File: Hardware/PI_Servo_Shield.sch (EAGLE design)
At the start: 80 parts, among them J1 RASPBERRYPI-40-PIN-GPIO, J19 QWIIC, J20 USB C, J21 Serial, Q1 2N7002PW, Q4 2N7002PW, U1 PCA9685, U3 CH340C

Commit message: Bumped the QWIIC label to 5mm package
didn't print very cleanly at the 3mm size on the protos from jlcpcb, so bumped it up to 5mm package.
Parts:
- U$1: value QWIIC_LOGO_3MM -> QWIIC_LOGO_5MM; device SparkFun-Aesthetics:QWIIC_LOGO_3MM -> SparkFun-Aesthetics:QWIIC_LOGO_5MM
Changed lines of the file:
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@@
 <grid distance="0.1" unitdist="inch" unit="inch" style="lines" multiple="1" display="no" altdistance="0.01" altunitdist="inch" altunit="inch"/>
 <layers>
-<layer number="1" name="Top" color="4" fill="1" visible="no" active="no"/>
-<layer number="2" name="Route2" color="1" fill="3" visible="no" active="no"/>
-<layer number="3" name="Route3" color="4" fill="3" visible="no" active="no"/>
-<layer number="4" name="Route4" color="1" fill="4" visible="no" active="no"/>
-<layer number="5" name="Route5" color="4" fill="4" visible="no" active="no"/>
-<layer number="6" name="Route6" color="1" fill="8" visible="no" active="no"/>
-<layer number="7" name="Route7" color="4" fill="8" visible="no" active="no"/>
-<layer number="8" name="Route8" color="1" fill="2" visible="no" active="no"/>
-<layer number="9" name="Route9" color="4" fill="2" visible="no" active="no"/>
-<layer number="10" name="Route10" color="1" fill="7" visible="no" active="no"/>
-<layer number="11" name="Route11" color="4" fill="7" visible="no" active="no"/>
-<layer number="12" name="Route12" color="1" fill="5" visible="no" active="no"/>
-<layer number="13" name="Route13" color="4" fill="5" visible="no" active="no"/>
-<layer number="14" name="Route14" color="1" fill="6" visible="no" active="no"/>
-<layer number="15" name="Route15" color="4" fill="6" visible="no" active="no"/>
-<layer number="16" name="Bottom" color="1" fill="1" visible="no" active="no"/>
-<layer number="17" name="Pads" color="2" fill="1" visible="no" active="no"/>
-<layer number="18" name="Vias" color="2" fill="1" visible="no" active="no"/>
-<layer number="19" name="Unrouted" color="6" fill="1" visible="no" active="no"/>
-<layer number="20" name="Dimension" color="15" fill="1" visible="no" active="no"/>
-<layer number="21" name="tPlace" color="16" fill="1" visible="no" active="no"/>
-<layer number="22" name="bPlace" color="14" fill="1" visible="no" active="no"/>
-<layer number="23" name="tOrigins" color="15" fill="1" visible="no" active="no"/>
-<layer number="24" name="bOrigins" color="15" fill="1" visible="no" active="no"/>
-<layer number="25" name="tNames" color="7" fill="1" visible="no" active="no"/>
-<layer number="26" name="bNames" color="7" fill="1" visible="no" active="no"/>
-<layer number="27" name="tValues" color="7" fill="1" visible="no" active="no"/>
-<layer number="28" name="bValues" color="7" fill="1" visible="no" active="no"/>
+<layer number="1" name="Top" color="4" fill="1" visible="yes" active="no"/>
+<layer number="2" name="Route2" color="1" fill="3" visible="yes" active="no"/>
+<layer number="3" name="Route3" color="4" fill="3" visible="yes" active="no"/>
+<layer number="4" name="Route4" color="1" fill="4" visible="yes" active="no"/>
+<layer number="5" name="Route5" color="4" fill="4" visible="yes" active="no"/>
+<layer number="6" name="Route6" color="1" fill="8" visible="yes" active="no"/>
+<layer number="7" name="Route7" color="4" fill="8" visible="yes" active="no"/>
+<layer number="8" name="Route8" color="1" fill="2" visible="yes" active="no"/>
+<layer number="9" name="Route9" color="4" fill="2" visible="yes" active="no"/>
+<layer number="10" name="Route10" color="1" fill="7" visible="yes" active="no"/>
+<layer number="11" name="Route11" color="4" fill="7" visible="yes" active="no"/>
+<layer number="12" name="Route12" color="1" fill="5" visible="yes" active="no"/>
+<layer number="13" name="Route13" color="4" fill="5" visible="yes" active="no"/>
+<layer number="14" name="Route14" color="1" fill="6" visible="yes" active="no"/>
+<layer number="15" name="Route15" color="4" fill="6" visible="yes" active="no"/>
+<layer number="16" name="Bottom" color="1" fill="1" visible="yes" active="no"/>
+<layer number="17" name="Pads" color="2" fill="1" visible="yes" active="no"/>
+<layer number="18" name="Vias" color="2" fill="1" visible="yes" active="no"/>
+<layer number="19" name="Unrouted" color="6" fill="1" visible="yes" active="no"/>
+<layer number="20" name="Dimension" color="15" fill="1" visible="yes" active="no"/>
+<layer number="21" name="tPlace" color="16" fill="1" visible="yes" active="no"/>
+<layer number="22" name="bPlace" color="14" fill="1" visible="yes" active="no"/>
+<layer number="23" name="tOrigins" color="15" fill="1" visible="yes" active="no"/>
+<layer number="24" name="bOrigins" color="15" fill="1" visible="yes" active="no"/>
+<layer number="25" name="tNames" color="7" fill="1" visible="yes" active="no"/>
+<layer number="26" name="bNames" color="7" fill="1" visible="yes" active="no"/>
+<layer number="27" name="tValues" color="7" fill="1" visible="yes" active="no"/>
+<layer number="28" name="bValues" color="7" fill="1" visible="yes" active="no"/>
 <layer number="29" name="tStop" color="7" fill="3" visible="no" active="no"/>
 <layer number="30" name="bStop" color="7" fill="6" visible="no" active="no"/>
@@
 <layer number="35" name="tGlue" color="7" fill="4" visible="no" active="no"/>
 <layer number="36" name="bGlue" color="7" fill="5" visible="no" active="no"/>
-<layer number="37" name="tTest" color="7" fill="1" visible="no" active="no"/>
-<layer number="38" name="bTest" color="7" fill="1" visible="no" active="no"/>
+<layer number="37" name="tTest" color="7" fill="1" visible="yes" active="no"/>
+<layer number="38" name="bTest" color="7" fill="1" visible="yes" active="no"/>
 <layer number="39" name="tKeepout" color="4" fill="11" visible="no" active="no"/>
 <layer number="40" name="bKeepout" color="1" fill="11" visible="no" active="no"/>
@@
 <layer number="44" name="Drills" color="7" fill="1" visible="no" active="no"/>
 <layer number="45" name="Holes" color="7" fill="1" visible="no" active="no"/>
-<layer number="46" name="Milling" color="3" fill="1" visible="no" active="no"/>
-<layer number="47" name="Measures" color="7" fill="1" visible="no" active="no"/>
-<layer number="48" name="Document" color="7" fill="1" visible="no" active="no"/>
-<layer number="49" name="Reference" color="7" fill="1" visible="no" active="no"/>
-<layer number="50" name="dxf" color="7" fill="1" visible="no" active="no"/>
-<layer number="51" name="tDocu" color="6" fill="1" visible="no" active="no"/>
-<layer number="52" name="bDocu" color="7" fill="1" visible="no" active="no"/>
-<layer number="53" name="tGND_GNDA" color="7" fill="9" visible="no" active="no"/>
-<layer number="54" name="bGND_GNDA" color="1" fill="9" visible="no" active="no"/>
-<layer number="56" name="wert" color="7" fill="1" visible="no" active="no"/>
-<layer number="57" name="tCAD" color="7" fill="1" visible="no" active="no"/>
-<layer number="59" name="tCarbon" color="7" fill="1" visible="no" active="no"/>
-<layer number="60" name="bCarbon" color="7" fill="1" visible="no" active="no"/>
+<layer number="46" name="Milling" color="3" fill="1" visible="yes" active="no"/>
+<layer number="47" name="Measures" color="7" fill="1" visible="yes" active="no"/>
+<layer number="48" name="Document" color="62" fill="7" visible="yes" active="no"/>
+<layer number="49" name="Reference" color="7" fill="1" visible="yes" active="no"/>
+<layer number="50" name="dxf" color="7" fill="1" visible="yes" active="no"/>
+<layer number="51" name="tDocu" color="6" fill="1" visible="yes" active="no"/>
+<layer number="52" name="bDocu" color="7" fill="1" visible="yes" active="no"/>
+<layer number="53" name="tGND_GNDA" color="7" fill="9" visible="yes" active="no"/>
+<layer number="54" name="bGND_GNDA" color="1" fill="9" visible="yes" active="no"/>
+<layer number="56" name="wert" color="7" fill="1" visible="yes" active="no"/>
+<layer number="57" name="tCAD" color="7" fill="1" visible="yes" active="no"/>
+<layer number="59" name="tCarbon" color="7" fill="1" visible="yes" active="no"/>
+<layer number="60" name="bCarbon" color="7" fill="1" visible="yes" active="no"/>
 <layer number="88" name="SimResults" color="9" fill="1" visible="no" active="yes"/>
 <layer number="89" name="SimProbes" color="9" fill="1" visible="no" active="yes"/>
@@
 <part name="GND1" library="SparkFun-PowerSymbols" deviceset="GND" device=""/>
 <part name="J21" library="SparkFun-Connectors" deviceset="CONN_04" device="LOCK" value="Serial"/>
-<part name="U$1" library="SparkFun-Aesthetics" deviceset="QWIIC_LOGO" device="_3MM"/>
+<part name="U$1" library="SparkFun-Aesthetics" deviceset="QWIIC_LOGO" device="_5MM" value="QWIIC_LOGO_5MM"/>
 <part name="C10" library="SparkFun-Capacitors" deviceset="0.1UF" device="-0603-25V-(+80/-20%)" value="0.1uF"/>
 <part name="GND24" library="SparkFun-PowerSymbols" deviceset="GND" device=""/>

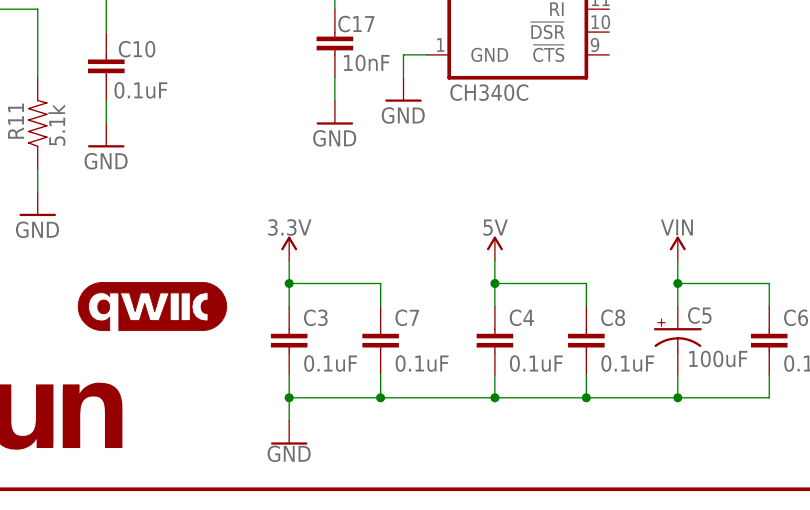
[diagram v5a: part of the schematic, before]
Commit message: Added 3.3V test point - gonna need this for properly testing the CH340
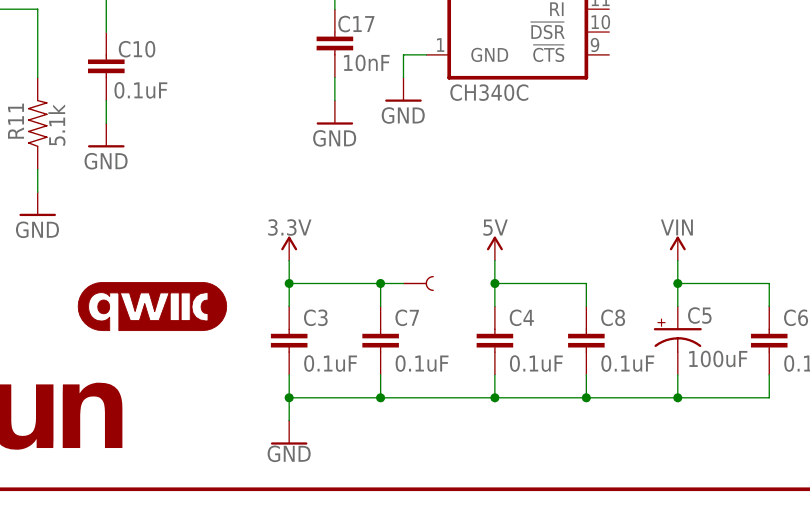
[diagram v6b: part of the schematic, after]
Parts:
- added TP22: TEST-POINT3X4, SparkFun-Connectors:TEST-POINT3X4
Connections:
- net 3.3V: now also TP22.1
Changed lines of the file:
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@@
 <grid distance="0.1" unitdist="inch" unit="inch" style="lines" multiple="1" display="no" altdistance="0.01" altunitdist="inch" altunit="inch"/>
 <layers>
-<layer number="1" name="Top" color="4" fill="1" visible="yes" active="no"/>
-<layer number="2" name="Route2" color="1" fill="3" visible="yes" active="no"/>
-<layer number="3" name="Route3" color="4" fill="3" visible="yes" active="no"/>
-<layer number="4" name="Route4" color="1" fill="4" visible="yes" active="no"/>
-<layer number="5" name="Route5" color="4" fill="4" visible="yes" active="no"/>
-<layer number="6" name="Route6" color="1" fill="8" visible="yes" active="no"/>
-<layer number="7" name="Route7" color="4" fill="8" visible="yes" active="no"/>
-<layer number="8" name="Route8" color="1" fill="2" visible="yes" active="no"/>
-<layer number="9" name="Route9" color="4" fill="2" visible="yes" active="no"/>
-<layer number="10" name="Route10" color="1" fill="7" visible="yes" active="no"/>
-<layer number="11" name="Route11" color="4" fill="7" visible="yes" active="no"/>
-<layer number="12" name="Route12" color="1" fill="5" visible="yes" active="no"/>
-<layer number="13" name="Route13" color="4" fill="5" visible="yes" active="no"/>
-<layer number="14" name="Route14" color="1" fill="6" visible="yes" active="no"/>
-<layer number="15" name="Route15" color="4" fill="6" visible="yes" active="no"/>
-<layer number="16" name="Bottom" color="1" fill="1" visible="yes" active="no"/>
-<layer number="17" name="Pads" color="2" fill="1" visible="yes" active="no"/>
-<layer number="18" name="Vias" color="2" fill="1" visible="yes" active="no"/>
-<layer number="19" name="Unrouted" color="6" fill="1" visible="yes" active="no"/>
-<layer number="20" name="Dimension" color="15" fill="1" visible="yes" active="no"/>
-<layer number="21" name="tPlace" color="16" fill="1" visible="yes" active="no"/>
-<layer number="22" name="bPlace" color="14" fill="1" visible="yes" active="no"/>
-<layer number="23" name="tOrigins" color="15" fill="1" visible="yes" active="no"/>
-<layer number="24" name="bOrigins" color="15" fill="1" visible="yes" active="no"/>
-<layer number="25" name="tNames" color="7" fill="1" visible="yes" active="no"/>
-<layer number="26" name="bNames" color="7" fill="1" visible="yes" active="no"/>
-<layer number="27" name="tValues" color="7" fill="1" visible="yes" active="no"/>
-<layer number="28" name="bValues" color="7" fill="1" visible="yes" active="no"/>
+<layer number="1" name="Top" color="4" fill="1" visible="no" active="no"/>
+<layer number="2" name="Route2" color="1" fill="3" visible="no" active="no"/>
+<layer number="3" name="Route3" color="4" fill="3" visible="no" active="no"/>
+<layer number="4" name="Route4" color="1" fill="4" visible="no" active="no"/>
+<layer number="5" name="Route5" color="4" fill="4" visible="no" active="no"/>
+<layer number="6" name="Route6" color="1" fill="8" visible="no" active="no"/>
+<layer number="7" name="Route7" color="4" fill="8" visible="no" active="no"/>
+<layer number="8" name="Route8" color="1" fill="2" visible="no" active="no"/>
+<layer number="9" name="Route9" color="4" fill="2" visible="no" active="no"/>
+<layer number="10" name="Route10" color="1" fill="7" visible="no" active="no"/>
+<layer number="11" name="Route11" color="4" fill="7" visible="no" active="no"/>
+<layer number="12" name="Route12" color="1" fill="5" visible="no" active="no"/>
+<layer number="13" name="Route13" color="4" fill="5" visible="no" active="no"/>
+<layer number="14" name="Route14" color="1" fill="6" visible="no" active="no"/>
+<layer number="15" name="Route15" color="4" fill="6" visible="no" active="no"/>
+<layer number="16" name="Bottom" color="1" fill="1" visible="no" active="no"/>
+<layer number="17" name="Pads" color="2" fill="1" visible="no" active="no"/>
+<layer number="18" name="Vias" color="2" fill="1" visible="no" active="no"/>
+<layer number="19" name="Unrouted" color="6" fill="1" visible="no" active="no"/>
+<layer number="20" name="Dimension" color="15" fill="1" visible="no" active="no"/>
+<layer number="21" name="tPlace" color="16" fill="1" visible="no" active="no"/>
+<layer number="22" name="bPlace" color="14" fill="1" visible="no" active="no"/>
+<layer number="23" name="tOrigins" color="15" fill="1" visible="no" active="no"/>
+<layer number="24" name="bOrigins" color="15" fill="1" visible="no" active="no"/>
+<layer number="25" name="tNames" color="7" fill="1" visible="no" active="no"/>
+<layer number="26" name="bNames" color="7" fill="1" visible="no" active="no"/>
+<layer number="27" name="tValues" color="7" fill="1" visible="no" active="no"/>
+<layer number="28" name="bValues" color="7" fill="1" visible="no" active="no"/>
 <layer number="29" name="tStop" color="7" fill="3" visible="no" active="no"/>
 <layer number="30" name="bStop" color="7" fill="6" visible="no" active="no"/>
@@
 <layer number="35" name="tGlue" color="7" fill="4" visible="no" active="no"/>
 <layer number="36" name="bGlue" color="7" fill="5" visible="no" active="no"/>
-<layer number="37" name="tTest" color="7" fill="1" visible="yes" active="no"/>
-<layer number="38" name="bTest" color="7" fill="1" visible="yes" active="no"/>
+<layer number="37" name="tTest" color="7" fill="1" visible="no" active="no"/>
+<layer number="38" name="bTest" color="7" fill="1" visible="no" active="no"/>
 <layer number="39" name="tKeepout" color="4" fill="11" visible="no" active="no"/>
 <layer number="40" name="bKeepout" color="1" fill="11" visible="no" active="no"/>
@@
 <layer number="44" name="Drills" color="7" fill="1" visible="no" active="no"/>
 <layer number="45" name="Holes" color="7" fill="1" visible="no" active="no"/>
-<layer number="46" name="Milling" color="3" fill="1" visible="yes" active="no"/>
-<layer number="47" name="Measures" color="7" fill="1" visible="yes" active="no"/>
-<layer number="48" name="Document" color="62" fill="7" visible="yes" active="no"/>
-<layer number="49" name="Reference" color="7" fill="1" visible="yes" active="no"/>
-<layer number="50" name="dxf" color="7" fill="1" visible="yes" active="no"/>
-<layer number="51" name="tDocu" color="6" fill="1" visible="yes" active="no"/>
-<layer number="52" name="bDocu" color="7" fill="1" visible="yes" active="no"/>
-<layer number="53" name="tGND_GNDA" color="7" fill="9" visible="yes" active="no"/>
-<layer number="54" name="bGND_GNDA" color="1" fill="9" visible="yes" active="no"/>
-<layer number="56" name="wert" color="7" fill="1" visible="yes" active="no"/>
-<layer number="57" name="tCAD" color="7" fill="1" visible="yes" active="no"/>
-<layer number="59" name="tCarbon" color="7" fill="1" visible="yes" active="no"/>
-<layer number="60" name="bCarbon" color="7" fill="1" visible="yes" active="no"/>
+<layer number="46" name="Milling" color="3" fill="1" visible="no" active="no"/>
+<layer number="47" name="Measures" color="7" fill="1" visible="no" active="no"/>
+<layer number="48" name="Document" color="62" fill="7" visible="no" active="no"/>
+<layer number="49" name="Reference" color="7" fill="1" visible="no" active="no"/>
+<layer number="50" name="dxf" color="7" fill="1" visible="no" active="no"/>
+<layer number="51" name="tDocu" color="6" fill="1" visible="no" active="no"/>
+<layer number="52" name="bDocu" color="7" fill="1" visible="no" active="no"/>
+<layer number="53" name="tGND_GNDA" color="7" fill="9" visible="no" active="no"/>
+<layer number="54" name="bGND_GNDA" color="1" fill="9" visible="no" active="no"/>
+<layer number="56" name="wert" color="7" fill="1" visible="no" active="no"/>
+<layer number="57" name="tCAD" color="7" fill="1" visible="no" active="no"/>
+<layer number="59" name="tCarbon" color="7" fill="1" visible="no" active="no"/>
+<layer number="60" name="bCarbon" color="7" fill="1" visible="no" active="no"/>
 <layer number="88" name="SimResults" color="9" fill="1" visible="no" active="yes"/>
 <layer number="89" name="SimProbes" color="9" fill="1" visible="no" active="yes"/>
@@
 <part name="Q4" library="SparkFun-DiscreteSemi" deviceset="MOSFET-NCH" device="-2N7002PW" value="2N7002PW"/>
 <part name="3.3V7" library="SparkFun-PowerSymbols" deviceset="VIN" device="" value="3.3V"/>
+<part name="TP22" library="SparkFun-Connectors" deviceset="TEST-POINT" device="3X4" value=""/>
 </parts>
 <sheets>
@@
 <attribute name="VALUE" x="198.12" y="145.034" size="1.778" layer="96" font="vector" rot="MR0" align="bottom-center"/>
 </instance>
+<instance part="TP22" gate="G$1" x="86.36" y="22.86" smashed="yes">
+<attribute name="VALUE" x="83.82" y="20.32" size="1.778" layer="96" font="vector"/>
+</instance>
 </instances>
 <busses>
@@
 <wire x1="73.66" y1="22.86" x2="73.66" y2="25.4" width="0.1524" layer="91"/>
 <junction x="73.66" y="22.86"/>
-</segment>
-<segment>
+<pinref part="TP22" gate="G$1" pin="1"/>
+<wire x1="86.36" y1="22.86" x2="83.82" y2="22.86" width="0.1524" layer="91"/>
+<junction x="83.82" y="22.86"/>
+</segment>
+<segment>

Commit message: Reverse current blocking diodes and more
-Added reverse current blocking circuits.
-Added auto switching isolation fet between Pi 5V rail and servo rail.
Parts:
- removed FRAME1: FRAME-LETTER, SparkFun-Aesthetics:FRAME-LETTER
- added FRAME2: FRAME-LEDGER, SparkFun-Aesthetics:FRAME-LEDGER
- added Q10, Q3, Q6, Q8: (no value), SparkFun-DiscreteSemi:TRANS_PNP_DUALSOT-363
- added Q11: (no value), SparkFun-DiscreteSemi:TRANS_NPN_DUAL-MBT3904DW1T1
- added Q12, Q2, Q5, Q7, Q9: 2.5A/30V/105mΩ, SparkFun-DiscreteSemi:MOSFET_PCH-DMG2307L
- added R13, R15, R19, R20, R21, R6, R8: 10k, SparkFun-Resistors:10KOHM-0603-1/10W-1%
- added R14, R3, R7, R9: 47k, SparkFun-Resistors:47KOHM-0603-1/10W-1%
- added R17, R18: 100, SparkFun-Resistors:100OHM-0603-1/4W-5%
- added S1: (no value), SparkFun-Switches:SWITCH-SPDT-PTH-11.6X4.0MM-LOCK
- added U2: SN74LVC1G32DCKR, SparkFun-IC-Logic:74LVC32DBV
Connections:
- net RXI renamed PI-TXO
- removed net 5V: C4.1, C8.1, J1.5V@2, J1.5V@4, J21.4, JP4.2, R1.2, R2.2, U1.VDD
- removed net TXO: D1.C, J1.RXI, J21.1, TP21.1, U3.TXO
- removed net VIN: C5.+, C6.1, F2.2, J10.2, J11.2, J12.2, J13.2, J14.2, J15.2, J16.2, J17.2, J18.2, J3.2, J4.2, J5.2, J6.2, J7.2, J8.2, J9.2, JP2.2, JP4.1, TP16.1
- new net CH340-TXO: D1.C, S1.S, U3.TXO
- new net N$1: Q5.G, Q6G$2.C, R7.2
- new net N$10: Q3G$1.B, Q3G$1.C, Q3G$2.B, R6.2
- new net N$11: Q6G$1.B, Q6G$1.C, Q6G$2.B, R8.2
- new net N$12: Q11Q1.B, Q11Q2.C, R18.1
- new net N$13: Q11Q1.C, Q12.G, R19.1
- new net N$15: Q7.G, Q8G$2.C, R9.2
- new net N$16: Q8G$1.B, Q8G$1.C, Q8G$2.B, R13.2
- new net N$17: R17.1, U2G1.Y
- new net N$18: Q10G$2.C, Q9.G, R14.2
- new net N$19: Q10G$1.B, Q10G$1.C, Q10G$2.B, R15.2
- new net N$8: Q11Q2.B, R17.2
- new net N$9: Q2.G, Q3G$2.C, R3.2
- new net PI-5V: C4.1, C8.1, J1.5V@2, J1.5V@4, JP4.2, Q10G$2.E, Q12.D, Q7.S, Q8G$2.E, Q9.S, R1.2, R18.2, R19.2, R2.2, U1.VDD
- new net PI-RXI: J1.RXI, S1.P, TP21.1
- new net RVR-5V: J21.4, Q2.D, Q3G$1.E, Q7.D, Q8G$1.E, R20.2, U2G1.A
- new net RVR-TXO: J21.1, S1.O
- new net SERVO: C5.+, C6.1, J10.2, J11.2, J12.2, J13.2, J14.2, J15.2, J16.2, J17.2, J18.2, J3.2, J4.2, J5.2, J6.2, J7.2, J8.2, J9.2, JP4.1, Q12.S, Q2.S, Q3G$2.E, Q5.S, Q6G$2.E, TP16.1
- new net USB-5V: F2.2, JP2.2, Q10G$1.E, Q5.D, Q6G$1.E, Q9.D, R21.2, U2G1.B
- net GND: now also Q11Q1.E, Q11Q2.E, R13.1, R14.1, R15.1, R20.1, R21.1, R3.1, R6.1, R7.1, R8.1, R9.1
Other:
- note added: "RXI"
- note added: "Reverse Current Protection"
- note added: "Selects which TX source (RVR or CH340) is connected to Raspi header RXI"
- note added: "Serial Swtich"
- note added: "TXO"
- note added: "~0V"
- moved on the sheet: C10, F2, J1, J10, J11, J12, J13, J14, J15, J16, J17, J18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
